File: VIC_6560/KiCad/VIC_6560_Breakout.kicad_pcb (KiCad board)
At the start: 2 copper layers, 23 x 64 mm, 3 parts, among them J1 MOTHERBOARD_VIC_SOCKET, J2 BREAKOUT_PINS, U1 6560/6561

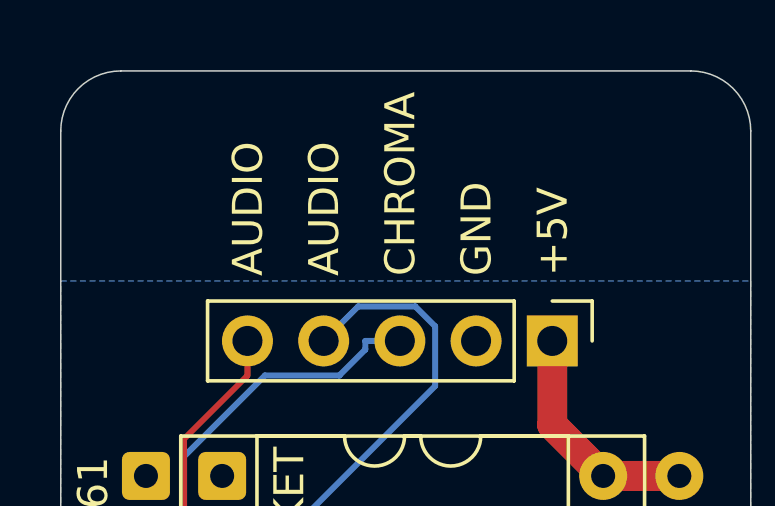
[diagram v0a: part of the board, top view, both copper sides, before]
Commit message: Corrected silkscreen
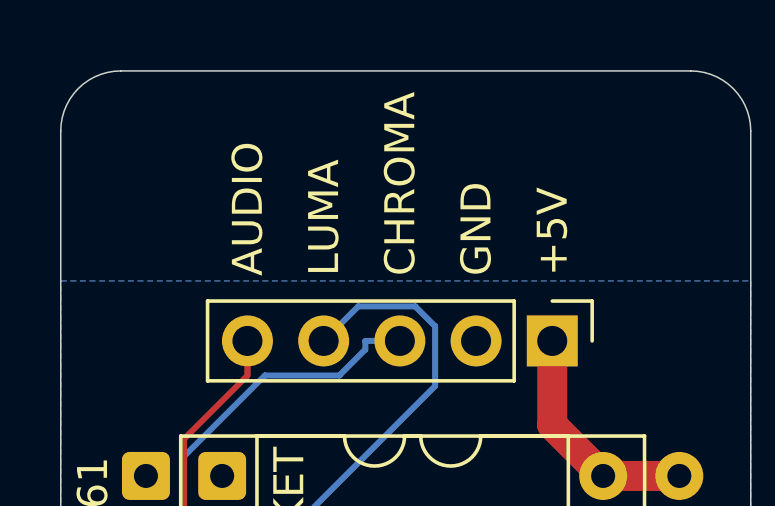
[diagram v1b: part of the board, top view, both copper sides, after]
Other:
- board text added: "LUMA"
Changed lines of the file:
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@@
 		)
 	)
-	(gr_text "AUDIO"
+	(gr_text "LUMA"
 		(at 62.985749 45.795378 90)
 		(layer "F.SilkS")
